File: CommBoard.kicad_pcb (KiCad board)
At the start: 2 copper layers, 132.1 x 86.4 mm, 77 parts, among them J1 RBUS, J2 Conn_Coaxial, J3 USB_C_Receptacle_USB2.0, J4 Conn_Coaxial, U1 ESP32-S3, U2 RFM95W-868S2, U3 RFM96W-433S2, U4 SN65HVD230, U5 LTC4411, U7 LTC4411, Y1 40MHz±10ppm

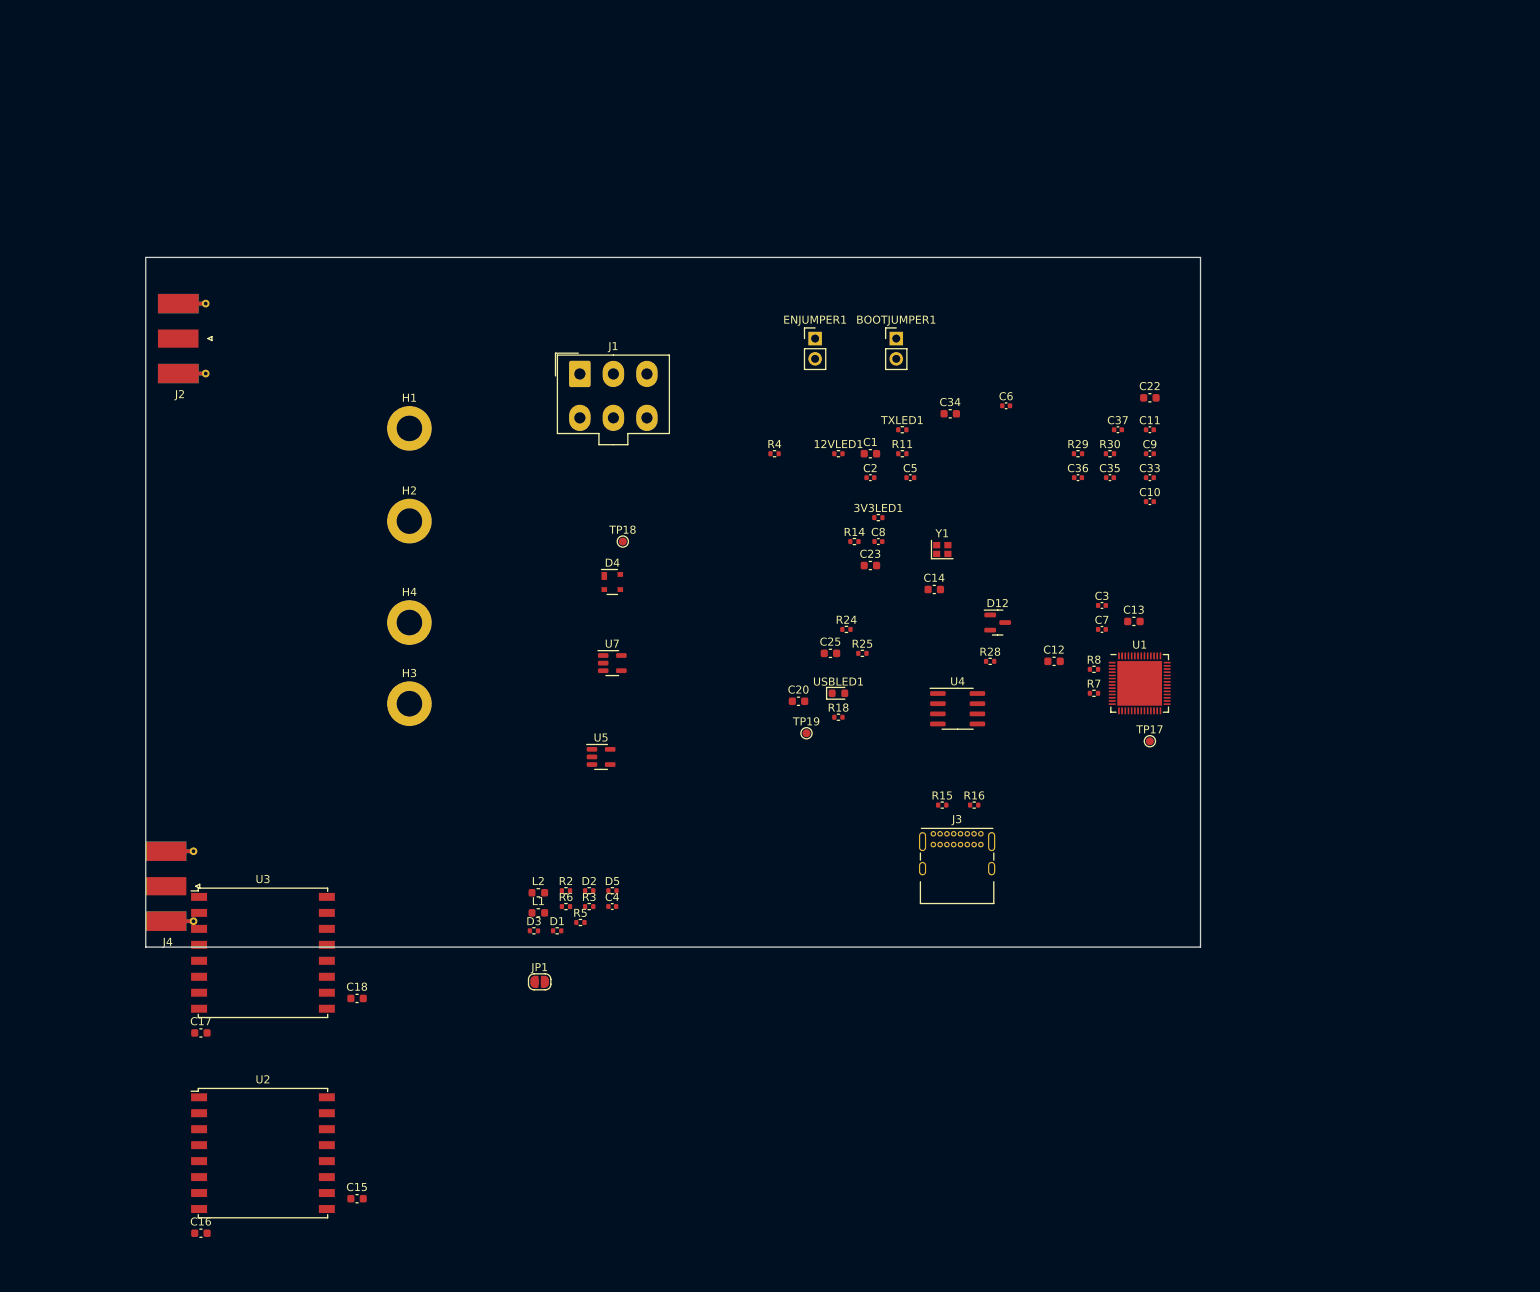
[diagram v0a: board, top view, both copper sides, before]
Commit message: PCB Component Grouping
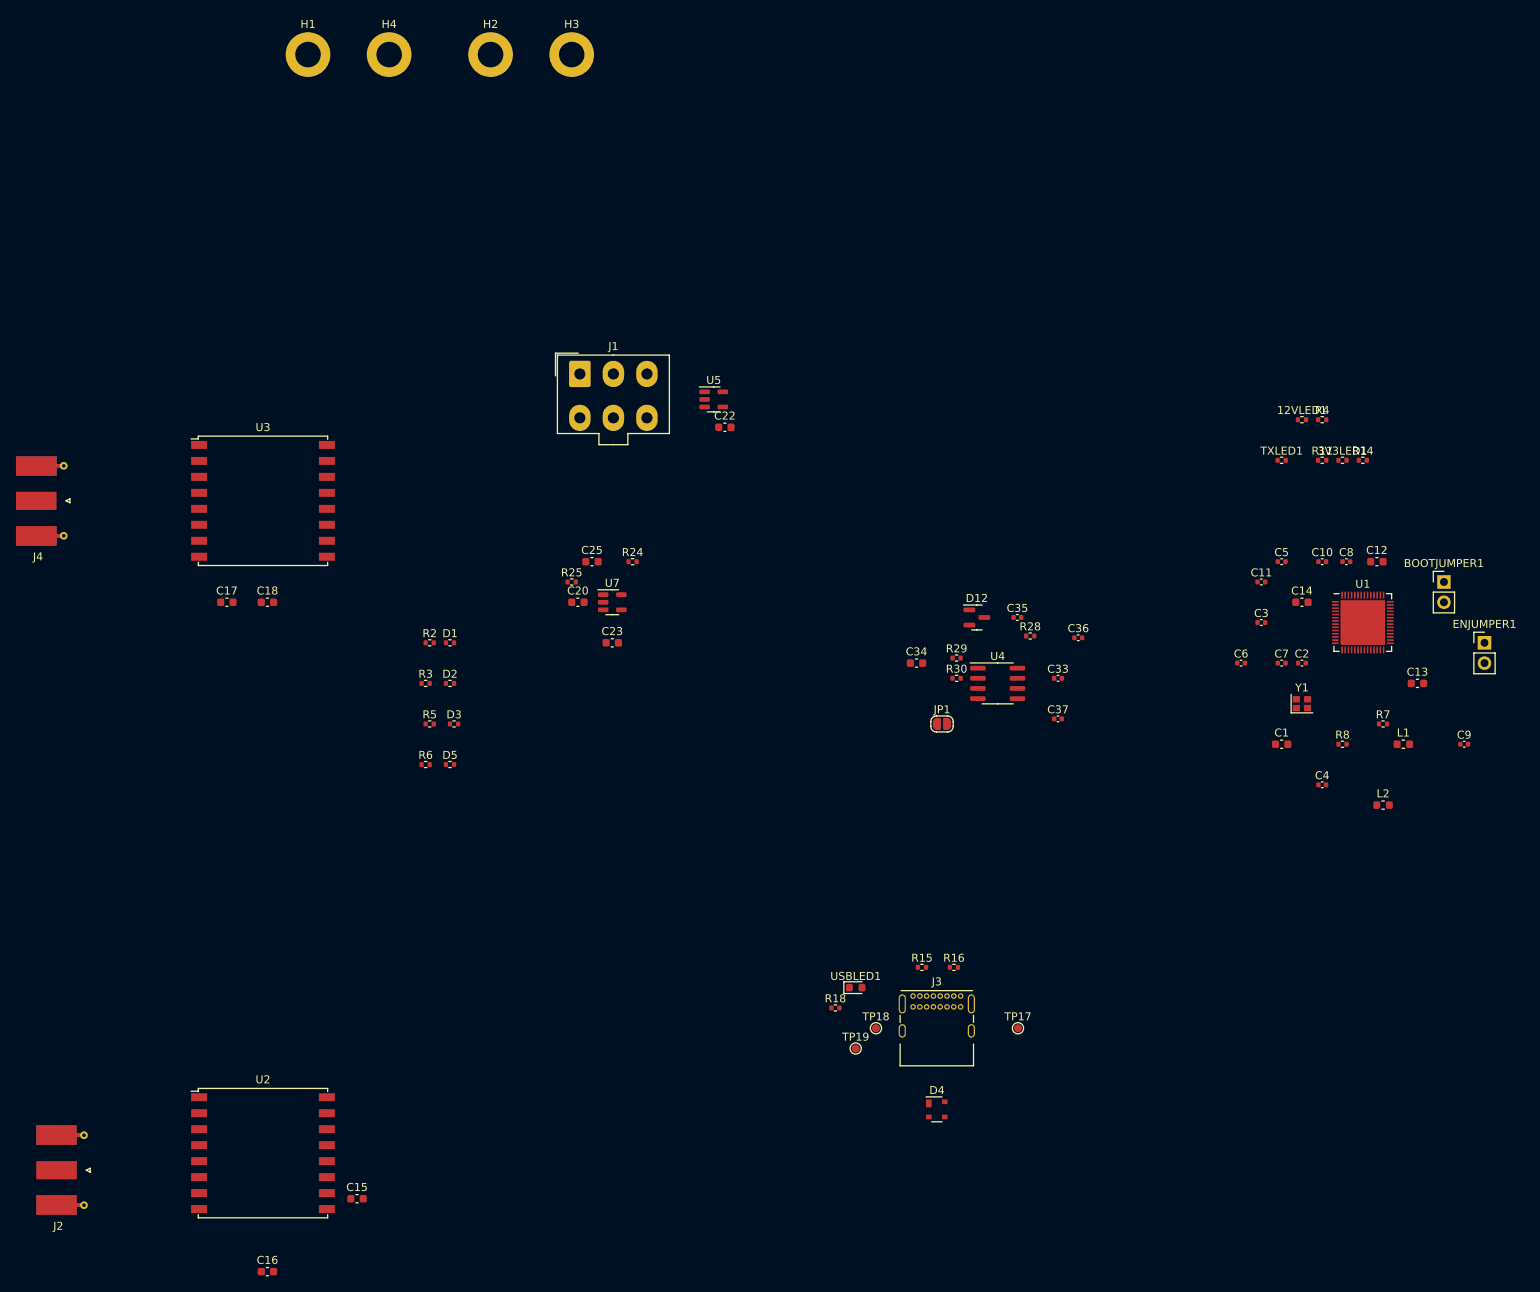
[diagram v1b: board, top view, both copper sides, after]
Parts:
- moved L1 110.4 mm to (205.7, 119.4)
- moved L2 106.3 mm to (203.2, 127.0)
- moved J2 105.2 mm to (38.8, 172.7)
- moved ENJUMPER1 92.1 mm to (215.9, 106.7)
- moved C4 90.2 mm to (195.6, 124.5)
- moved H3 83.8 mm to (101.6, 33.0)
- moved D4 77.5 mm to (147.3, 165.1)
- moved BOOTJUMPER1 75.0 mm to (210.8, 99.1)
- moved H4 71.2 mm to (78.7, 33.0)
- moved R4 68.7 mm to (195.6, 78.7)
- moved TP18 68.7 mm to (139.7, 154.9)
- moved R14 64.5 mm to (200.7, 83.8)
- moved C1 63.1 mm to (190.5, 119.4)
- moved JP1 59.8 mm to (148.0, 116.8)
- moved H2 59.3 mm to (91.4, 33.0)
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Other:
- board outline removed
- copper layers 2 -> 4

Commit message: New Template Update
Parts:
- removed C33: 100nF, Capacitor_SMD:C_0402_1005Metric
- removed C34: 10uF, Capacitor_SMD:C_0603_1608Metric
- removed C35: 0.1uF, Capacitor_SMD:C_0402_1005Metric
- removed C36: 220pF, Capacitor_SMD:C_0402_1005Metric
- removed C37: 220 pF, Capacitor_SMD:C_0402_1005Metric
- removed D12: SM712_SOT23, Package_TO_SOT_SMD:SOT-23
- removed R24: 56k, Resistor_SMD:R_0402_1005Metric
- removed R25, R28: 10k, Resistor_SMD:R_0402_1005Metric
- removed R29, R30: 60, Resistor_SMD:R_0402_1005Metric
- removed TP17, TP18, TP19: TestPoint, TestPoint:TestPoint_Pad_D1.0mm
- added C19: 220pF, Capacitor_SMD:C_0402_1005Metric, F.Cu at (112.7, 80.8)
- added C21: 0.1uF, Capacitor_SMD:C_0402_1005Metric, F.Cu at (221.3, 105.3)
- added C24: 4.7uF, Capacitor_SMD:C_0402_1005Metric, F.Cu at (112.5, 70.4)
- added C26: 1uF, Capacitor_SMD:C_0402_1005Metric, F.Cu at (170.7, 85.6)
- added C27: 22uF, Capacitor_SMD:C_0402_1005Metric, F.Cu at (175.5, 88.2)
- added C28: 10uF, Capacitor_SMD:C_0402_1005Metric, F.Cu at (180.1, 83.4)
- added C29: 4.7uF, Capacitor_SMD:C_0402_1005Metric, F.Cu at (178.0, 83.4)
- added C30: 10uF, Capacitor_SMD:C_0402_1005Metric, F.Cu at (177.1, 92.7)
- added C31: 0.1uF, Capacitor_SMD:C_0402_1005Metric, F.Cu at (177.1, 91.8)
- added C32: 0.1uF, Capacitor_SMD:C_0402_1005Metric, F.Cu at (240.8, 126.1)
- added D6: LED_Small, Resistor_SMD:R_0402_1005Metric, F.Cu at (267.6, 87.8)
- added L3: 1uH, Inductor_SMD:L_0805_2012Metric, F.Cu at (173.0, 90.8)
- added R1: 10K, Resistor_SMD:R_0402_1005Metric, F.Cu at (78.4, 72.1)
- added R10: 60, Resistor_SMD:R_0402_1005Metric, F.Cu at (109.4, 80.5)
- added R12: 5.1k, Resistor_SMD:R_0402_1005Metric, F.Cu at (70.6, 86.2)
- added R13: 470, Resistor_SMD:R_0402_1005Metric, F.Cu at (69.4, 95.6)
- added R17: 56k, Resistor_SMD:R_0402_1005Metric, F.Cu at (179.0, 91.8)
- added R19: 470, Resistor_SMD:R_0402_1005Metric, F.Cu at (267.6, 92.8)
- added R20: 470, Resistor_SMD:R_0402_1005Metric, F.Cu at (271.6, 87.8)
- added R9: 60, Resistor_SMD:R_0402_1005Metric, F.Cu at (113.7, 76.9)
- added TP1: TestPoint, TestPoint:TestPoint_Pad_D1.0mm, F.Cu at (66.5, 91.1)
- added TP2: TestPoint, TestPoint:TestPoint_Pad_D1.0mm, F.Cu at (66.5, 94.2)
- added TP3: TestPoint, TestPoint:TestPoint_Pad_D1.0mm, F.Cu at (69.5, 91.1)
- added TP4: TestPoint, TestPoint:TestPoint_Pad_D1.5mm, F.Cu at (106.4, 70.7)
- added TP5: TestPoint, TestPoint:TestPoint_Pad_D1.5mm, F.Cu at (119.6, 59.7)
- added TP6: TestPoint, TestPoint:TestPoint_Pad_D1.5mm, F.Cu at (115.6, 62.2)
- added TP7: TestPoint, TestPoint:TestPoint_Pad_D1.5mm, F.Cu at (111.6, 64.1)
- added TP8: TestPoint, TestPoint:TestPoint_Pad_D1.5mm, F.Cu at (111.6, 67.7)
- added U6: LM66100, Package_TO_SOT_SMD:SOT-23-5, F.Cu at (107.2, 66.7)
- added U8: SC4215, iclr:SOIC127P599X175-9N, F.Cu at (179.0, 87.6)
- C1, C16: value 0.1uF -> 10uF; footprint Capacitor_SMD:C_0603_1608Metric -> Capacitor_SMD:C_0402_1005Metric
- C12: value C -> 4.2pF; footprint Capacitor_SMD:C_0603_1608Metric -> Capacitor_SMD:C_0402_1005Metric
- C13, C14, C20, C23, C25: footprint Capacitor_SMD:C_0603_1608Metric -> Capacitor_SMD:C_0402_1005Metric
- C15: value 10uF -> 100nF; footprint Capacitor_SMD:C_0603_1608Metric -> Capacitor_SMD:C_0402_1005Metric
- C17: value 10uF -> 0.1uF; footprint Capacitor_SMD:C_0603_1608Metric -> Capacitor_SMD:C_0402_1005Metric
- C18: value 0.1uF -> 220pF; footprint Capacitor_SMD:C_0603_1608Metric -> Capacitor_SMD:C_0402_1005Metric
- C22: value 4.7uF -> 10uF; footprint Capacitor_SMD:C_0603_1608Metric -> Capacitor_SMD:C_0402_1005Metric
- C4: value 10uF -> 1uF
- C5, C8: value 1uF -> 0.1uF
- C7: value 0.1uF -> 1uF
- D1: value LED_Small -> SM712_SOT23; footprint Resistor_SMD:R_0402_1005Metric -> Package_TO_SOT_SMD:SOT-23
- D2: value LED_Small -> SP0503BAHT; footprint Resistor_SMD:R_0402_1005Metric -> Package_TO_SOT_SMD:SOT-143
- D4: value SP0503BAHT -> LED_Small; footprint Package_TO_SOT_SMD:SOT-143 -> Resistor_SMD:R_0402_1005Metric
- J2: value Conn_Coaxial -> USB_C_Receptacle_USB2.0; footprint Connector_Coaxial:SMA_Molex_73251-1153_EdgeMount_Horizontal -> Connector_USB:USB_C_Receptacle_GCT_USB4085
- J3: value USB_C_Receptacle_USB2.0 -> Conn_Coaxial; footprint Connector_USB:USB_C_Receptacle_GCT_USB4085 -> Connector_Coaxial:SMA_Molex_73251-1153_EdgeMount_Horizontal
- L1, L2: footprint Inductor_SMD:L_0603_1608Metric -> Inductor_SMD:L_0402_1005Metric
- R11: value 470 -> 5.1k
- R15: value 5.1k -> 470
- R16: value 5.1k -> 14k
- R18: value 470 -> 10k
- R3: value 470 -> 10K
- R4: value 3k -> 470
- R5: value 470 -> 47.5
- R6: value 470 -> 499
- R7: value 10K -> 3k
- R8: value 10K -> 0
- U2: value RFM95W-868S2 -> SN65HVD230; footprint RF_Module:HOPERF_RFM9XW_SMD -> Package_SO:SOIC-8_3.9x4.9mm_P1.27mm
- U3: value RFM96W-433S2 -> RFM95W-868S2
- U4: value SN65HVD230 -> RFM96W-433S2; footprint Package_SO:SOIC-8_3.9x4.9mm_P1.27mm -> RF_Module:HOPERF_RFM9XW_SMD
- U5: value LTC4411 -> LM66100
- U7: value LTC4411 -> MAX77827AEFD+T; footprint Package_TO_SOT_SMD:SOT-23-5 -> iclr:CONV_MAX77827AEFD+T
- USBLED1: footprint LED_SMD:LED_0603_1608Metric -> Resistor_SMD:R_0402_1005Metric
- moved J4 211.7 mm to (245.9, 118.1), turned to 180 degrees
- moved D5 179.6 mm to (263.6, 93.0)
- moved D3 179.1 mm to (263.6, 87.8)
- moved U3 166.3 mm to (229.1, 95.3)
- moved ENJUMPER1 151.7 mm to (71.5, 60.2)
- moved U1 145.5 mm to (58.0, 75.6)
- moved C9 145.0 mm to (73.7, 80.4)
- moved L1 143.2 mm to (67.9, 80.4)
- moved BOOTJUMPER1 140.2 mm to (76.2, 60.2)
- moved C20 138.5 mm to (240.8, 101.0)
- moved D4 138.2 mm to (263.6, 90.4)
- moved R15 134.8 mm to (267.6, 90.3)
- moved L2 134.6 mm to (87.1, 58.9)
- moved Y1 133.0 mm to (64.5, 79.9)
- moved C13 133.0 mm to (81.3, 70.0)
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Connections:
- net Net-(J1-Pad3) renamed RBUS_uC_V
- C1 pad 1: /CHIP_PU -> +3V3
- C17 pad 1: +3V3 -> Net-(C17-Pad1)
- C18 pad 1: +3V3 -> GND
- C18 pad 2: GND -> /CAN+
- C20 pad 1: GND -> +3V3
- C20 pad 2: VBUS -> GND
- C23 pad 1: +3V3 -> /Power/BBIN
- C25 pad 1: GND -> /Power/BBIN
- C25 pad 2: Net-(C25-Pad2) -> GND
- C3 pad 1: /BOOT -> /CHIP_PU
- C6 pad 1: +3V3 -> Net-(C6-Pad1)
- C7 pad 1: Net-(C7-Pad1) -> +3V3
- C8 pad 1: +3V3 -> /BOOT
- D1 pad 1: GND -> /CAN-
- D1 pad 2: Net-(D1-Pad2) -> /CAN+
- D2 pad 2: Net-(D2-Pad2) -> VBUS
- D4 pad 2: VBUS -> Net-(D4-Pad2)
- JP1 pad 2: Net-(C35-Pad1) -> Net-(C17-Pad1)
- L1 pad 2: Net-(C7-Pad1) -> Net-(C6-Pad1)
- R11 pad 1: +3V3 -> Net-(J2-PadA5)
- R11 pad 2: Net-(R11-Pad2) -> GND
- R14 pad 1: Net-(3V3LED1-Pad2) -> Net-(D3-Pad2)
- R14 pad 2: +3V3 -> /R95_TX
- R15 pad 1: Net-(J3-PadA5) -> Net-(D4-Pad2)
- R15 pad 2: GND -> /R95_RX
- R16 pad 1: GND -> /Power/SEL
- R16 pad 2: Net-(J3-PadB5) -> GND
- R18 pad 1: VBUS -> /Power/FBIn
- R18 pad 2: Net-(R18-Pad2) -> GND
- R2 pad 1: Net-(D1-Pad2) -> +3V3
- R2 pad 2: /R95_TX -> Net-(R2-Pad2)
- R3 pad 1: Net-(D2-Pad2) -> +3V3
- R3 pad 2: /R95_RX -> /BOOT
- R4 pad 1: +12V -> Net-(3V3LED1-Pad2)
- R4 pad 2: Net-(12VLED1-Pad2) -> +3V3
- R5 pad 1: Net-(D3-Pad2) -> GND
- R5 pad 2: /R96_TX -> Net-(C12-Pad1)
- R6 pad 1: Net-(D5-Pad2) -> /TXD
- R6 pad 2: /R96_RX -> Net-(R6-Pad2)
- R7 pad 1: +3V3 -> +12V
- R7 pad 2: /CHIP_PU -> Net-(12VLED1-Pad2)
- R8 pad 1: +3V3 -> Net-(R8-Pad1)
- R8 pad 2: /BOOT -> GND
- TXLED1 pad 2: Net-(R11-Pad2) -> Net-(R2-Pad2)
- U1 pad 2: Net-(C7-Pad1) -> Net-(C6-Pad1)
- U1 pad 3: Net-(C7-Pad1) -> Net-(C6-Pad1)
- U1 pad 45: /TXD -> unconnected-(U1-Pad45)
- U1 pad 49: unconnected-(U1-Pad49) -> Net-(R6-Pad2)
- U2 pad 1: GND -> /CAN_TX
- U2 pad 2: /MOSI -> GND
- U2 pad 3: /MISO -> +3V3
- U2 pad 4: /SCK -> /CAN_RX
- U2 pad 5: /R95_NSS -> /CAN-BUS/Vref
- U2 pad 6: /R95_RESET -> /CAN-
- U2 pad 7: unconnected-(U2-Pad7) -> /CAN+
- U2 pad 8: GND -> Net-(R8-Pad1)
- U3 pad 14: /R96_DIO0 -> /R95_DIO0
- U3 pad 2: /MISO -> /MOSI
- U3 pad 3: /MOSI -> /MISO
- U3 pad 5: /R96_NSS -> /R95_NSS
- U3 pad 6: /R96_RESET -> /R95_RESET
- U3 pad 9: Net-(J4-Pad1) -> Net-(J3-Pad1)
- U4 pad 1: /CAN_TX -> GND
- U4 pad 2: GND -> /MISO
- U4 pad 3: +3V3 -> /MOSI
- U4 pad 4: /CAN_RX -> /SCK
- U4 pad 5: /CAN-BUS/Vref -> /R96_NSS
- U4 pad 6: /CAN- -> /R96_RESET
- U4 pad 7: /CAN+ -> unconnected-(U4-Pad7)
- U4 pad 8: Net-(R28-Pad1) -> GND
- U5 pad 5: +3V3 -> /Power/BBIN
- U7 pad 1: Net-(C25-Pad2) -> /Power/SEL
- U7 pad 2: GND -> unconnected-(U7-Pad2)
- U7 pad 3: GND -> /Power/BBIN
- U7 pad 4: unconnected-(U7-Pad4) -> GND
- U7 pad 5: +3V3 -> /Power/BIAS
- USBLED1 pad 2: Net-(R18-Pad2) -> Net-(R13-Pad2)
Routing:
- net /Power/BBOUT: track 0.00 -> 12.3 mm
- net GND: track 0.00 -> 6.29 mm, vias 0 -> 7
- net /CAN+: track 0.00 -> 3.30 mm
- net /Power/FBIn: track 0.00 -> 2.61 mm
- net /Power/BBIN: track 0.00 -> 2.00 mm
- net +3V3: track 0.00 -> 1.61 mm, vias 0 -> 1
- net /Power/BIAS: track 0.00 -> 1.42 mm
- net /Power/SEL: track 0.00 -> 1.01 mm
- net /Power/LX2: vias 0 -> 7
- net /Power/LX1: vias 0 -> 7
- added copper zone on F.Cu, net +3V3
- added copper zone on F.Cu, net /Power/BBIN
- added copper zone on F.Cu, net /Power/BBOUT
- added copper zone on B.Cu, net /Power/LX1
- added copper zone on F.Cu, net /Power/LX1
- added copper zone on B.Cu, net /Power/LX2
- added copper zone on F.Cu, net /Power/LX2
- added copper zone on F.Cu, net GND

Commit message: New Routing
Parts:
- moved H1 159.8 mm to (220.0, 31.1)
- moved H2 147.2 mm to (220.0, 63.1)
- moved J2 141.0 mm to (194.0, 57.1)
- moved TP2 138.1 mm to (197.0, 49.1)
- moved D2 138.0 mm to (201.0, 54.1), turned to -90 degrees
- moved TP3 137.1 mm to (200.0, 49.1)
- moved USBLED1 135.0 mm to (195.0, 44.1)
- moved R13 135.0 mm to (195.0, 46.1)
- moved R11 134.3 mm to (198.1, 46.1)
- moved R12 134.3 mm to (198.1, 44.1)
- moved TP1 134.3 mm to (193.9, 49.1)
- moved J3 95.3 mm to (174.0, 32.8), turned to -90 degrees
- moved J4 92.7 mm to (209.6, 32.8), turned to -90 degrees
- moved H3 88.8 mm to (162.0, 63.1)
- moved H4 85.5 mm to (162.0, 31.1)
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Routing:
- net Net-(C17-Pad1): track 0.00 -> 9.70 mm, vias 0 -> 2
- net /CAN-: track 0.00 -> 7.41 mm
- net GND: track 6.29 -> 13.5 mm, vias 7 -> 8
- net /CAN+: track 3.30 -> 9.76 mm
- net Net-(C13-Pad1): track 0.00 -> 5.53 mm
- net +3V3: track 1.61 -> 6.72 mm
- net Net-(L2-Pad1): track 0.00 -> 4.82 mm
- net Net-(C6-Pad1): track 0.00 -> 4.50 mm
- net /CAN-BUS/Vref: track 0.00 -> 2.48 mm
- net Net-(C14-Pad1): track 0.00 -> 2.33 mm
- added copper zone on In2.Cu, net +3V3
- added copper zone on In1.Cu, net GND
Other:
- board outline added: 64 x 38 mm

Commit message: Grouping 2
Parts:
- moved R14 80.9 mm to (170.3, 63.1), turned to 180 degrees
- moved R15 77.0 mm to (170.3, 61.6), turned to 180 degrees
- moved TP6 71.2 mm to (178.2, 96.1)
- moved D4 70.7 mm to (172.5, 61.6), turned to 180 degrees
- moved D3 70.7 mm to (172.5, 63.1), turned to 180 degrees
- moved TP8 64.6 mm to (175.1, 79.2)
- moved TP4 56.5 mm to (160.0, 88.6)
- moved U6 55.4 mm to (155.6, 93.6)
- moved U5 53.3 mm to (155.6, 89.7)
- moved C24 46.8 mm to (152.8, 94.3), turned to 90 degrees
- moved TP7 46.1 mm to (147.7, 92.8)
- moved C1 45.3 mm to (49.8, 74.8), turned to 90 degrees
- moved C12 44.4 mm to (50.2, 71.2)
- moved R3 43.5 mm to (50.3, 78.6)
- moved C23 43.4 mm to (152.8, 90.4), turned to 90 degrees
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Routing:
- net Net-(R8-Pad1): track 0.00 -> 8.24 mm
- net Net-(C12-Pad2): track 0.00 -> 4.60 mm
- net Net-(C17-Pad1): track 9.70 -> 12.1 mm
- net /CAN_TX: track 0.00 -> 2.22 mm, vias 0 -> 1
- net /CAN_RX: track 0.00 -> 2.07 mm, vias 0 -> 1
- net GND: track 13.5 -> 11.5 mm, vias 8 -> 9
- net Net-(R6-Pad2): track 0.00 -> 1.40 mm, vias 0 -> 1
- net +3V3: track 6.72 -> 5.78 mm
- net Net-(L2-Pad1): track 4.82 -> 4.28 mm
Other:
- board size 64 x 38 mm -> 66 x 40 mm
- board text added: "RFM95-868MHz"
- board text added: "RFM96-433MHz"

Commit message: Most compressed board you'll see
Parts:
- moved C7 145.7 mm to (196.4, 42.0)
- moved C9 145.7 mm to (195.4, 42.0)
- moved C11 143.8 mm to (199.0, 52.1)
- moved C1 143.8 mm to (190.8, 46.6)
- moved C2 143.8 mm to (191.3, 49.3)
- moved C4 143.8 mm to (190.8, 44.6)
- moved R1 143.8 mm to (191.3, 48.2)
- moved Y1 143.8 mm to (198.6, 39.6)
- moved C10 143.8 mm to (202.4, 42.4)
- moved C13 143.8 mm to (200.6, 39.6)
- moved C14 143.8 mm to (198.7, 37.6)
- moved C5 143.8 mm to (191.9, 46.6)
- moved C6 143.8 mm to (191.9, 44.6)
- moved L1 143.8 mm to (193.0, 44.6)
- moved L2 143.8 mm to (196.6, 39.6)
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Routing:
- net GND: track 11.5 -> 13.4 mm
- net Net-(J2-PadA5): vias 0 -> 1
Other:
- board size 66 x 40 mm -> 66 x 42 mm
